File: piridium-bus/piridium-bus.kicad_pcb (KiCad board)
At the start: 2 copper layers, 90.2 x 95.9 mm, 129 parts, among them J1 EPS, J2 MODEM UART, J3 INHIBITS, J4 ANT, J5 PAYLOAD, J6 IN1, J7 IN2, J8 IN1, J9 IN2, Q1 DMP3015LSSQ, Q2 Si4186DY, Q3 DMP3015LSSQ, Q4 Si4186DY, Q5 DMP3015LSSQ, Q6 DMP3015LSSQ, Q7 2N7002, Q8 DMP3015LSSQ, U1 LM1117-3.3, U10 INA180A3, U11 LT3652EMSE, U12 INA180A3, U2 TPS54394RSAR, U3 MAX6369, U4 74HC126, U5 INA180A3, U6 DS3232M, U7 INA180A3, U8 MCP3208, U9 LT3652EMSE

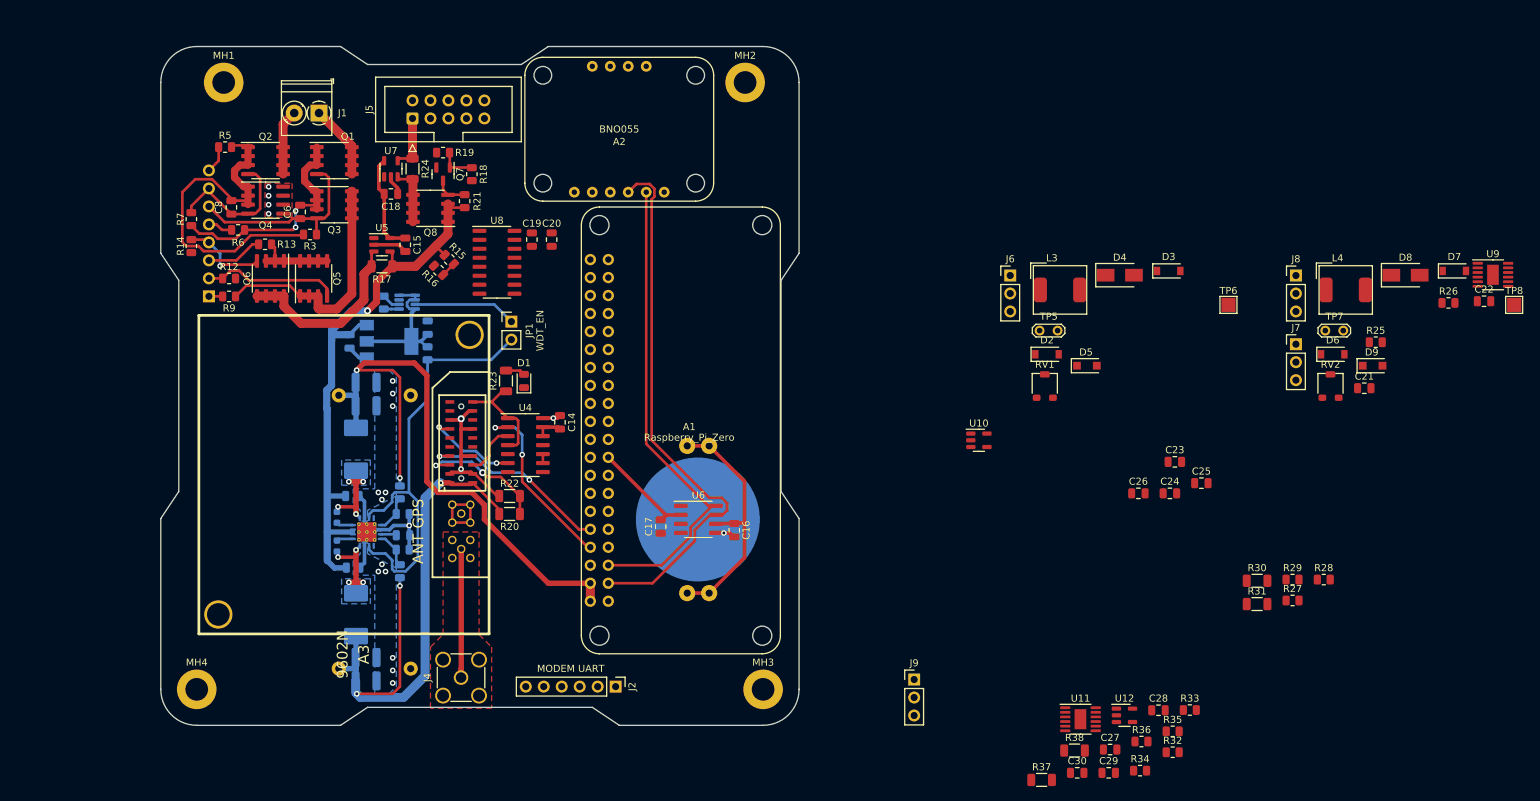
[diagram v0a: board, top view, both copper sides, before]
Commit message: route data lines, begin to route MPPT circuitry
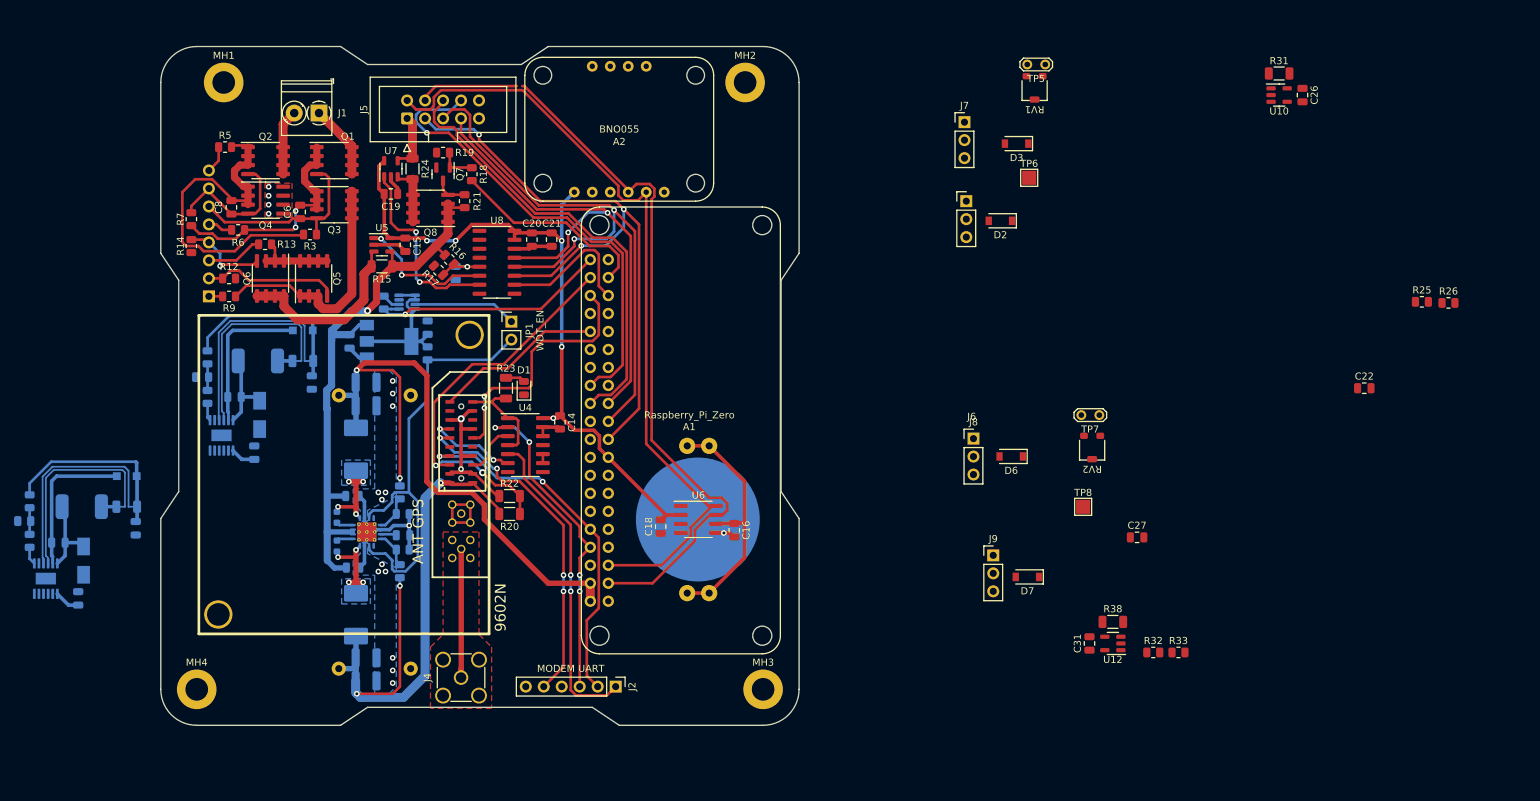
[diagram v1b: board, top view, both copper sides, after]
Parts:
- added C17: 0.1uF, Capacitor_SMD:C_0805_2012Metric, B.Cu at (143.3, 82.8)
- C23: renamed from C22; moved to B.Cu
- C24: renamed from C23; moved to B.Cu
- C25: renamed from C24; moved to B.Cu
- C28: renamed from C27; moved to B.Cu
- C29: renamed from C28; moved to B.Cu
- C30: renamed from C29; moved to B.Cu
- D4, D5, D8, D9, L3, L4, R27, R28, R29, R30, R34, R35, R36, R37, U11, U9: moved to B.Cu
- moved D8 191.1 mm to (90.7, 123.4), turned to -90 degrees
- moved L4 181.2 mm to (90.4, 115.8)
- moved U9 181.0 mm to (110.2, 105.7), turned to 90 degrees
- moved D9 176.7 mm to (96.8, 111.5)
- moved C23 175.0 mm to (114.8, 108.2), turned to 90 degrees
- moved R35 164.7 mm to (83.1, 115.0), turned to 90 degrees
- moved R36 160.9 mm to (82.3, 117.8)
- moved R28 160.8 mm to (108.2, 94.7), turned to 90 degrees
- moved R34 160.2 mm to (83.1, 120.6), turned to -90 degrees
- moved C29 157.2 mm to (87.1, 120.9), turned to 180 degrees
- moved R29 156.7 mm to (107.4, 97.5)
- moved R27 156.0 mm to (108.2, 100.3), turned to -90 degrees
- moved U11 147.5 mm to (85.4, 126.0), turned to 90 degrees
- moved C28 147.3 mm to (89.9, 128.8), turned to 90 degrees
- moved C30 141.7 mm to (98.1, 118.9), turned to -90 degrees
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- renumbered C17 to C18, C18 to C19, C19 to C20, C20 to C21, C21 to C22, C25 to C26, C26 to C27, C30 to C31, R17 to R15, R15 to R16, R16 to R17
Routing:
- net SPI_MOSI: track 0.00 -> 89.9 mm, vias 0 -> 3
- net SPI_MISO: track 0.00 -> 84.8 mm, vias 0 -> 2
- net SPI_SCK: track 0.00 -> 74.0 mm, vias 0 -> 2
- net +3.3V: track 32.2 -> 100.3 mm, vias 1 -> 5
- net SPI_CE1: track 0.00 -> 66.6 mm, vias 0 -> 1
- net SPI_CE0: track 0.00 -> 63.3 mm
- net Net-(C25-Pad1): track 0.00 -> 58.2 mm
- net Net-(C30-Pad1): track 0.00 -> 58.0 mm
- net UART_CTS: track 0.00 -> 48.5 mm, vias 0 -> 4
- net UART_RTS: track 0.00 -> 45.0 mm, vias 0 -> 2
- net I2C_SCL: track 67.3 -> 111.2 mm
- net S_MODEM_ON_OFF: track 18.7 -> 57.1 mm
- net S_RING_INDICATOR: track 0.00 -> 35.7 mm, vias 0 -> 2
- net I2C_SDA: track 77.4 -> 112.9 mm
- net S_HANDSHAKE: track 2.26 -> 35.0 mm, vias 0 -> 1
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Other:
- outline, holes or cut-outs redrawn

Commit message: route solar
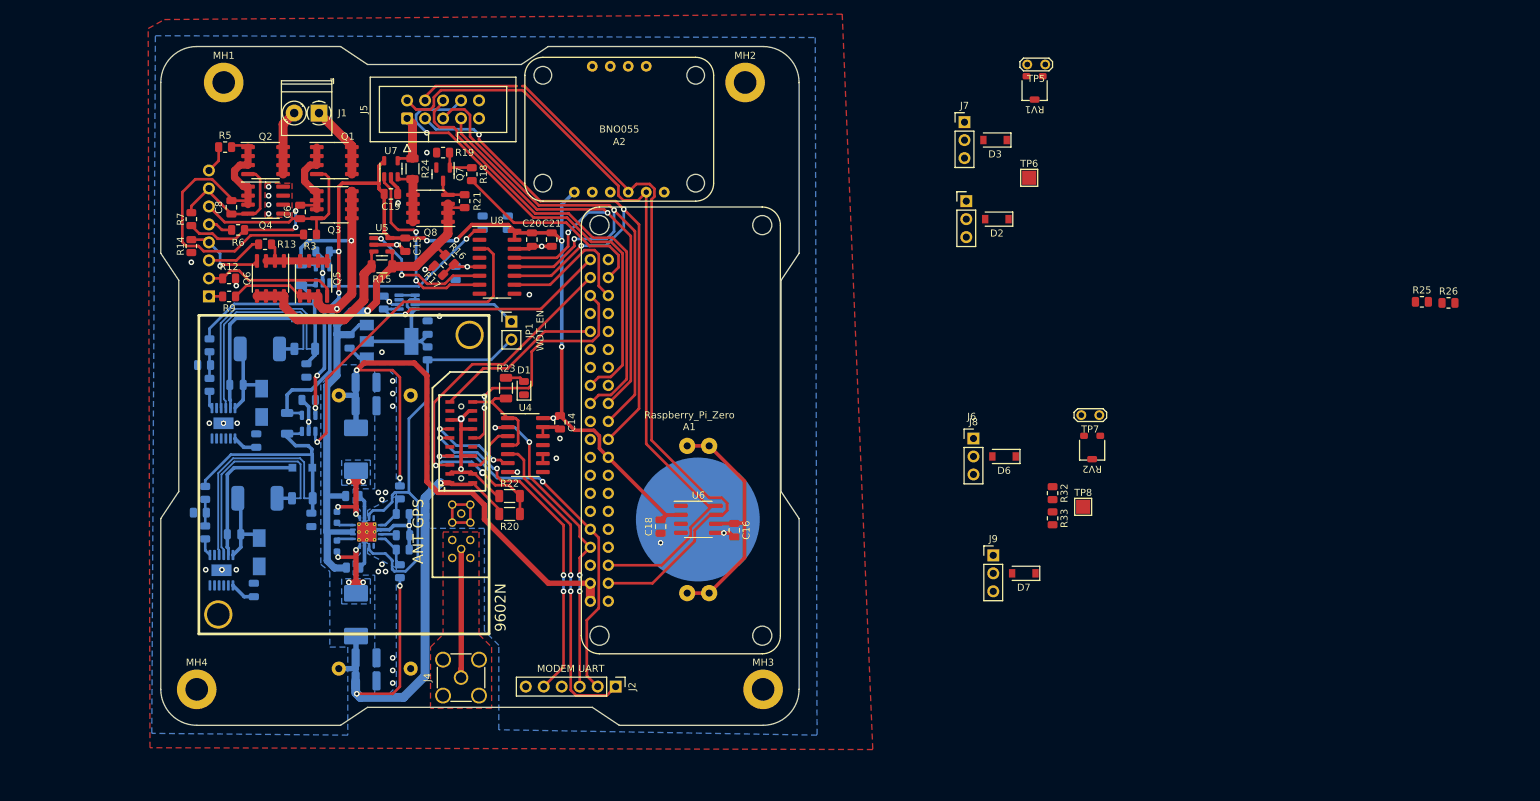
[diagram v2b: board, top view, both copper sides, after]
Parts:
- C22, C26, C27, C31, R31, R38, U10, U12: moved to B.Cu
- moved R31 141.1 mm to (121.4, 83.1), turned to -90 degrees
- moved C26 140.2 mm to (124.5, 79.8), turned to 180 degrees
- moved U10 137.5 mm to (124.5, 83.1), turned to 90 degrees
- moved C22 126.7 mm to (147.1, 75.7), turned to 90 degrees
- moved R38 120.0 mm to (119.4, 104.0), turned to -90 degrees
- moved U12 117.8 mm to (122.5, 104.0), turned to 90 degrees
- moved C31 115.5 mm to (122.5, 100.7), turned to 180 degrees
- moved C27 99.4 mm to (150.6, 75.7), turned to 90 degrees
- moved R32 26.6 mm to (227.6, 113.9), turned to -90 degrees
- moved R33 26.0 mm to (227.6, 117.5), turned to -90 degrees
- moved C28 24.8 mm to (114.7, 127.6)
- moved C30 24.8 mm to (122.9, 117.7)
- moved D8 24.8 mm to (115.5, 122.2)
- moved L4 24.8 mm to (115.2, 114.6)
- moved R34 24.8 mm to (107.9, 119.4)
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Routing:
- net /I_OUT_B: track 0.00 -> 47.7 mm, vias 0 -> 1
- net +3.3V: track 100.3 -> 144.5 mm, vias 5 -> 9
- net /CHARGE_OUT: track 38.2 -> 71.8 mm, vias 0 -> 2
- net /I_OUT_A: track 0.00 -> 24.7 mm, vias 0 -> 1
- net GND: track 69.0 -> 82.5 mm, vias 20 -> 43
- net Net-(C30-Pad1): track 58.0 -> 64.6 mm
- net Net-(C25-Pad1): track 58.2 -> 63.7 mm
- net +BATT: track 82.5 -> 81.3 mm
- added copper zone on In1.Cu, net GND
- added copper zone on In2.Cu, net GND
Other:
- copper layers 2 -> 4

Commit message: finish routing
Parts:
- RV1, RV2, TP5, TP6, TP7, TP8: moved to B.Cu
- moved RV1 129.7 mm to (106.7, 109.7), turned to 0 degrees
- moved TP5 129.5 mm to (105.4, 99.1), turned to -90 degrees
- moved TP7 126.7 mm to (113.8, 142.2), turned to 90 degrees
- moved TP6 123.6 mm to (106.2, 105.7), turned to 180 degrees
- moved TP8 119.9 mm to (113.8, 136.4), turned to 90 degrees
- moved RV2 119.0 mm to (116.8, 132.3), turned to -90 degrees
- moved J8 113.8 mm to (104.1, 124.7)
- moved D6 111.1 mm to (113.0, 136.1)
- moved R32 109.5 mm to (120.7, 137.4), turned to 90 degrees
- moved D7 107.4 mm to (117.1, 140.0), turned to -90 degrees
- moved R33 106.8 mm to (122.7, 137.4)
- moved J9 104.4 mm to (117.1, 144.3), turned to 90 degrees
- moved R26 104.0 mm to (179.8, 78.2)
- moved R25 100.1 mm to (179.8, 80.3), turned to 180 degrees
- moved J6 84.2 mm to (171.2, 144.3), turned to 90 degrees
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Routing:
- net Net-(C23-Pad1): track 3.51 -> 195.0 mm, vias 0 -> 5
- net /V_IN_B: track 0.00 -> 86.9 mm, vias 0 -> 1
- net /V_IN_A: track 0.00 -> 46.6 mm, vias 0 -> 2
- net Net-(C28-Pad1): track 3.61 -> 31.7 mm, vias 0 -> 3
- net +3.3V: track 144.5 -> 165.8 mm
- net Net-(RV1-Pad2): track 0.00 -> 13.6 mm
- net Net-(D6-Pad2): track 0.00 -> 13.0 mm
- net Net-(RV2-Pad2): track 0.00 -> 11.7 mm
- net Net-(D7-Pad2): track 0.00 -> 3.73 mm
- net GND: track 82.5 -> 86.0 mm, vias 43 -> 48
- net Net-(D3-Pad2): track 0.00 -> 2.67 mm
- net Net-(D2-Pad2): track 0.00 -> 2.67 mm
- net I2C_SDA: track 112.9 -> 113.7 mm

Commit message: cleanup silkscreen
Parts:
- moved C26 3.88 mm to (128.3, 79.6)
- moved U10 3.88 mm to (128.3, 82.9)
- moved R31 3.88 mm to (125.3, 82.9)
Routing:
- net +3.3V: track 165.8 -> 170.4 mm
- net /CHARGE_OUT: track 71.8 -> 68.1 mm
- net /I_OUT_A: track 24.7 -> 21.5 mm
- net GND: track 86.0 -> 87.0 mm
- net Net-(Q6-Pad5): track 26.0 -> 26.7 mm, vias 0 -> 1
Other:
- board text added: "+"
- board text added: "-"
- board text added: "BATTERY"
- board text added: "Board Comments"
- board text added: "CR2032 RTC Backup"
- board text added: "GND"
- board text added: "HS INH"
- board text added: "HS RBF"
- board text added: "Inhibit Connector Bridged - Power Disconnect"
- board text added: "LS RBF"
- board text added: "PAYLOAD CONNECTOR"
- board text added: "Piridium Avionics Board github.com/Alan-JH/piridium-bus v1"
- board text added: "RTS"
- board text added: "Solar Input A1"
- board text added: "Solar Input A2"
- board text added: "Solar Input B1"
- board text added: "Solar Input B2"

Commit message: battery sch finish
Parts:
- added C32: 0.1uF, Capacitor_SMD:C_0805_2012Metric, F.Cu at (217.4, 91.4)
- added C33: 10uF, Capacitor_SMD:C_0805_2012Metric, F.Cu at (222.8, 87.0)
- added C34: 0.1uF, Capacitor_SMD:C_0805_2012Metric, F.Cu at (217.4, 109.3)
- added C35: 10uF, Capacitor_SMD:C_0805_2012Metric, F.Cu at (222.8, 104.8)
- added Q10: 2N7002, Package_TO_SOT_SMD:SOT-23, F.Cu at (218.1, 87.7)
- added Q11: 2N7002, Package_TO_SOT_SMD:SOT-23, F.Cu at (212.5, 95.5)
- added Q12: DMP3015LSSQ, Package_SO:SOIC-8_3.9x4.9mm_P1.27mm, F.Cu at (205.8, 106.6)
- added Q13: 2N7002, Package_TO_SOT_SMD:SOT-23, F.Cu at (218.1, 105.6)
- added Q14: 2N7002, Package_TO_SOT_SMD:SOT-23, F.Cu at (212.5, 113.3)
- added Q9: DMP3015LSSQ, Package_SO:SOIC-8_3.9x4.9mm_P1.27mm, F.Cu at (205.8, 88.7)
- added R18: 6K, Resistor_SMD:R_0805_2012Metric, F.Cu at (237.6, 87.0)
- added R19: 4K, Resistor_SMD:R_0805_2012Metric, F.Cu at (233.2, 89.9)
- added R43: 10K, Resistor_SMD:R_0805_2012Metric, F.Cu at (217.1, 94.7)
- added R44: 510K, Resistor_SMD:R_0805_2012Metric, F.Cu at (221.6, 94.4)
- added R45: 10K, Resistor_SMD:R_0805_2012Metric, F.Cu at (217.1, 97.7)
- added R46: 10K, Resistor_SMD:R_0805_2012Metric, F.Cu at (221.9, 91.4)
- added R47: 10m, Resistor_SMD:R_1206_3216Metric, F.Cu at (212.9, 87.1)
- added R48: 10K, Resistor_SMD:R_0805_2012Metric, F.Cu at (217.1, 112.5)
- added R49: 510K, Resistor_SMD:R_0805_2012Metric, F.Cu at (221.6, 112.3)
- added R50: 10K, Resistor_SMD:R_0805_2012Metric, F.Cu at (217.1, 115.5)
- added R51: 10K, Resistor_SMD:R_0805_2012Metric, F.Cu at (221.9, 109.3)
- added R52: 10m, Resistor_SMD:R_1206_3216Metric, F.Cu at (212.9, 105.0)
- added R7: 6K, Resistor_SMD:R_0805_2012Metric, F.Cu at (237.6, 89.9)
- added R8: 4K, Resistor_SMD:R_0805_2012Metric, F.Cu at (233.2, 87.0)
- added U13: SN74LVC1G14DBV, Package_TO_SOT_SMD:SOT-23-5, F.Cu at (212.6, 91.0)
- added U14: MAX4373F, Package_SO:SO-8_3.9x4.9mm_P1.27mm, F.Cu at (205.8, 95.2)
- added U15: SN74LVC1G14DBV, Package_TO_SOT_SMD:SOT-23-5, F.Cu at (212.6, 108.8)
- added U16: MAX4373F, Package_SO:SO-8_3.9x4.9mm_P1.27mm, F.Cu at (205.8, 113.0)
- renumbered C15 to C14, C16 to C15, C17 to C16, C14 to C17, C20 to C19, C5 to C2, C21 to C20, C19 to C21, C6 to C3, C8 to C4, C2 to C5, C3 to C6, C4 to C7, C7 to C8, J3 to J2, J2 to J3, R3 to R1, R8 to R10, R9 to R11, R10 to R15, R11 to R16, R15 to R17, R4 to R2, R16 to R20, R17 to R21, R18 to R22, R19 to R23, R21 to R24, R24 to R25, R20 to R26, R22 to R27, R23 to R28, R25 to R29, R5 to R3, R26 to R30, R27 to R31, R28 to R32, R29 to R33, R30 to R34, R31 to R35, R32 to R36, R33 to R37, R34 to R38, R35 to R39, R1 to R4, R36 to R40, R37 to R41, R38 to R42, R2 to R5, R7 to R9, TP4 to TP3, TP3 to TP4, U3 to U2, U2 to U3, U5 to U4, U4 to U5, U8 to U7, U7 to U8
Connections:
- net Net-(C5-Pad1) renamed +3.3VA
- C12 pad 1: +5VP -> /5VP LCL/POWER_IN
- C13 pad 1: +5VP -> /5VP LCL/POWER_IN
- C5 pad 1: +5V -> /5V LCL/POWER_IN
- C6 pad 1: +5V -> /5V LCL/POWER_IN
- L1 pad 1: +5V -> /5V LCL/POWER_IN
- L2 pad 2: +5VP -> /5VP LCL/POWER_IN
- R15 pad 1: +5VP -> /5VP LCL/POWER_IN
- R4 pad 1: +5V -> /5V LCL/POWER_IN
- TP1 pad 1: +5V -> /5V LCL/POWER_IN
- TP4 pad 1: +5VP -> /5VP LCL/POWER_IN
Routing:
- net +5V: track 91.3 -> 2.54 mm, vias 2 -> 0
- net +5VP: track 84.2 -> 10.6 mm, vias 3 -> 1
- net /5VP LCL/POWER_IN: track 0.00 -> 70.5 mm, vias 0 -> 2
- net /5V LCL/POWER_IN: track 0.00 -> 70.1 mm, vias 0 -> 2
